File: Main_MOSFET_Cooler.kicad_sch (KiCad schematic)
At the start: 18 parts, among them J1 Gate, J2 MOS+, J3 MOS-, J4 Thermister, P1 Eoshi-chan_Silk, P2 Serial_QR, Q1 TK100E06N1, Q2 TK100E06N1

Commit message: before mirror
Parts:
- H1: footprint (none) -> MountingHole:MountingHole_3.2mm_M3
- R1: footprint (none) -> Resistor_SMD:R_0603_1608Metric

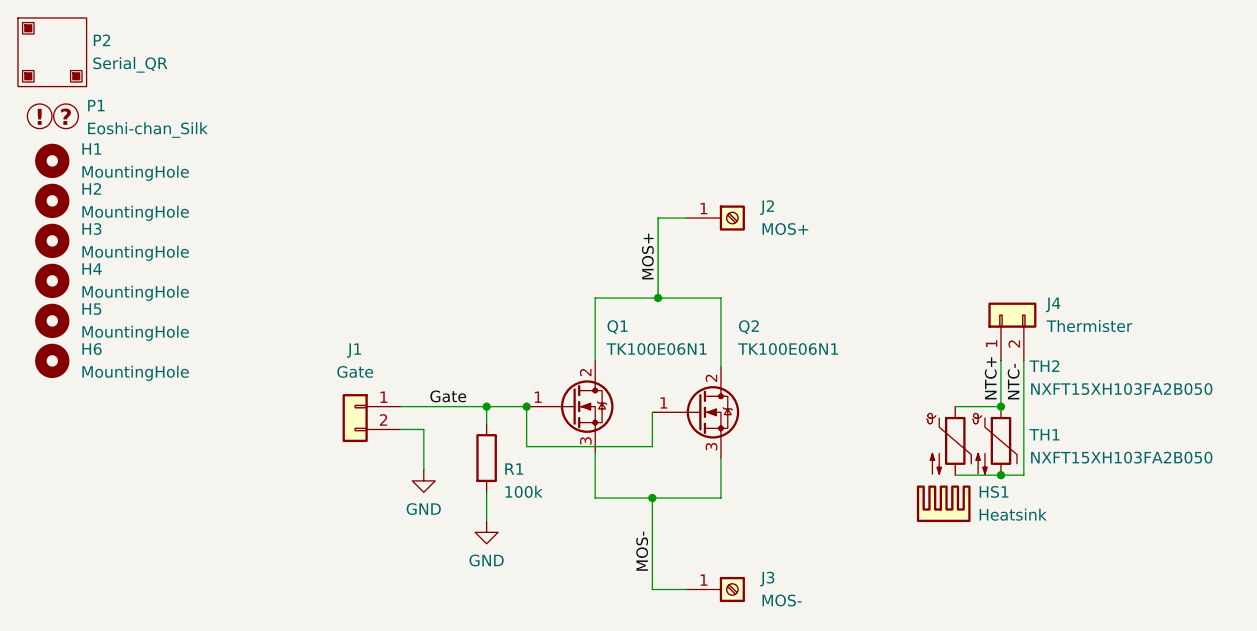
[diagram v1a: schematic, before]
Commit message: added 5.45mm pitch version
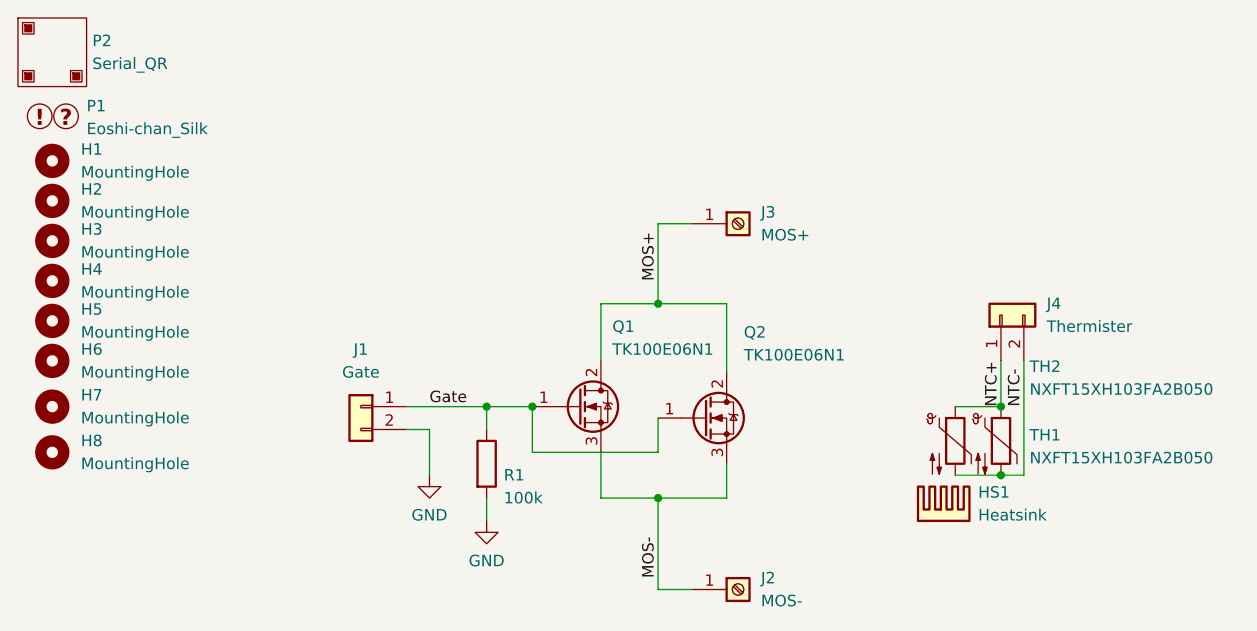
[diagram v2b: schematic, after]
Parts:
- added H7, H8: MountingHole, MountingHole:MountingHole_3.2mm_M3, symbol Mechanical:MountingHole
- J1: footprint Connector_JST:JST_XH_S2B-XH-A_1x02_P2.50mm_Horizontal -> Connector_JST:JST_XH_B2B-XH-A_1x02_P2.50mm_Vertical
- J2: value MOS+ -> MOS-; footprint Akizuki_ScrewTerminal:ScrewTerminal_01x01_PCB-20 -> AM_Conn_ScrewTerminal:ScrewTerminal_01x01_PCB-20
- J3: value MOS- -> MOS+; footprint Akizuki_ScrewTerminal:ScrewTerminal_01x01_PCB-20 -> AM_Conn_ScrewTerminal:ScrewTerminal_01x01_PCB-20
- J4: footprint Connector_JST:JST_XH_B2B-XH-A_1x02_P2.50mm_Vertical -> Connector_JST:JST_XH_S2B-XH-A_1x02_P2.50mm_Horizontal
- Q1, Q2: footprint Package_TO_SOT_THT:TO-220-3_Horizontal_TabDown -> Package_TO_SOT_THT:TO-220-3_Horizontal_TabUp
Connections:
- net MOS+: now also J3.1 (Pin_1); no longer J2.1 (Pin_1)
- net MOS-: now also J2.1 (Pin_1); no longer J3.1 (Pin_1)
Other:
- moved on the sheet: J1, J2, J3, Q1, Q2, R1
